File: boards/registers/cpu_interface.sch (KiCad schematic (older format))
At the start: 9 parts, among them J3 IO, U30 74AC20, U31 28C256, U32 62256-TSOP, U33 74ACT02

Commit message: PCB attempt
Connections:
- net a0: now also J3.4 (Pin_4), U32.15 (A2); no longer J3.3 (Pin_3), U32.17 (A0)
- net a1: now also J3.3 (Pin_3); no longer J3.4 (Pin_4)
- net a11: now also U32.5 (A13); no longer U32.2 (A11)
- net a12: now also U32.4 (A8); no longer U32.9 (A12)
- net a13: now also U32.3 (A9); no longer U32.5 (A13)
- net a14: now also U32.2 (A11); no longer U32.8 (A14)
- net a2: now also J3.6 (Pin_6), U32.17 (A0); no longer J3.5 (Pin_5), U32.15 (A2)
- net a3: now also J3.5 (Pin_5); no longer J3.6 (Pin_6)
- net a4: now also J3.8 (Pin_8); no longer J3.7 (Pin_7)
- net a5: now also J3.7 (Pin_7); no longer J3.8 (Pin_8)
- net a6: now also J3.10 (Pin_10); no longer J3.9 (Pin_9)
- net a7: now also J3.9 (Pin_9); no longer J3.10 (Pin_10)
- net a8: now also U32.9 (A12); no longer U32.4 (A8)
- net a9: now also U32.8 (A14); no longer U32.3 (A9)
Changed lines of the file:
@@
 	6000 3200 5550 3200
 Text Label 5650 1800 2    50   ~ 0
-a0
+a2
 Text Label 5550 1900 0    50   ~ 0
 a1
 Text Label 5550 2000 0    50   ~ 0
-a2
+a0
 Text Label 5550 2100 0    50   ~ 0
 a3
@@
 a6
 Text Label 5550 2600 0    50   ~ 0
-a8
+a12
 Text Label 5550 2500 0    50   ~ 0
 a7
 Text Label 5550 2700 0    50   ~ 0
-a9
+a13
 Text Label 5550 2800 0    50   ~ 0
 a10
 Text Label 5550 2900 0    50   ~ 0
+a14
+Text Label 5550 3000 0    50   ~ 0
+a8
+Text Label 5550 3100 0    50   ~ 0
 a11
-Text Label 5550 3000 0    50   ~ 0
-a12
-Text Label 5550 3100 0    50   ~ 0
-a13
 Text Label 5550 3200 0    50   ~ 0
-a14
+a9
 Wire Bus Line
 	5450 1200 2800 1200
@@
 	9200 1800 9450 1800
 Text Label 9250 1500 0    50   ~ 0
+a1
+Text Label 9250 1600 0    50   ~ 0
+a3
+Text Label 9250 1700 0    50   ~ 0
+a5
+Text Label 9250 1800 0    50   ~ 0
+a7
+Text Label 10100 1500 0    50   ~ 0
 a0
-Text Label 9250 1600 0    50   ~ 0
+Text Label 10100 1600 0    50   ~ 0
 a2
-Text Label 9250 1700 0    50   ~ 0
+Text Label 10100 1700 0    50   ~ 0
 a4
-Text Label 9250 1800 0    50   ~ 0
+Text Label 10100 1800 0    50   ~ 0
 a6
-Text Label 10100 1500 0    50   ~ 0
-a1
-Text Label 10100 1600 0    50   ~ 0
-a3
-Text Label 10100 1700 0    50   ~ 0
-a5
-Text Label 10100 1800 0    50   ~ 0
-a7
 $Comp
 L Connector_Generic:Conn_02x13_Odd_Even J3

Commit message: CPU registers board
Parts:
- removed C33: 0.1u, Capacitor_SMD:C_0805_2012Metric, symbol Device:C
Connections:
- net a0: now also J3.17 (Pin_17); no longer J3.4 (Pin_4)
- net a1: now also J3.18 (Pin_18); no longer J3.3 (Pin_3)
- net a2: now also J3.19 (Pin_19); no longer J3.6 (Pin_6)
- net a3: now also J3.20 (Pin_20); no longer J3.5 (Pin_5)
- net a4: now also J3.21 (Pin_21); no longer J3.8 (Pin_8)
- net a5: now also J3.22 (Pin_22); no longer J3.7 (Pin_7)
- net a6: now also J3.23 (Pin_23); no longer J3.10 (Pin_10)
- net a7: now also J3.24 (Pin_24); no longer J3.9 (Pin_9)
- net clk: now also J3.7 (Pin_7); no longer J3.19 (Pin_19)
- net d0: now also J3.16 (Pin_16), U32.26 (D7); no longer J3.11 (Pin_11), U32.18 (D0)
- net d1: now also J3.15 (Pin_15), U32.25 (D6); no longer J3.12 (Pin_12), U32.19 (D1)
- net d2: now also J3.14 (Pin_14), U32.24 (D5); no longer J3.13 (Pin_13), U32.20 (D2)
- net d3: now also J3.13 (Pin_13), U32.23 (D4); no longer J3.14 (Pin_14), U32.22 (D3)
- net d4: now also J3.12 (Pin_12), U32.22 (D3); no longer J3.15 (Pin_15), U32.23 (D4)
- net d5: now also J3.11 (Pin_11), U32.20 (D2); no longer J3.16 (Pin_16), U32.24 (D5)
- net d6: now also J3.10 (Pin_10), U32.19 (D1); no longer J3.17 (Pin_17), U32.25 (D6)
- net d7: now also J3.9 (Pin_9), U32.18 (D0); no longer J3.18 (Pin_18), U32.26 (D7)
- net ~io_cs: now also J3.4 (Pin_4); no longer J3.20 (Pin_20)
- net ~io_rdy: now also J3.3 (Pin_3); no longer J3.24 (Pin_24)
- net ~oe: now also J3.5 (Pin_5); no longer J3.21 (Pin_21)
- net ~rst: now also J3.8 (Pin_8); no longer J3.22 (Pin_22)
- net ~we: now also J3.6 (Pin_6); no longer J3.23 (Pin_23)
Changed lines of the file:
@@
 	7000 2500 7250 2500
 Text Label 7100 1800 0    50   ~ 0
+d7
+Text Label 7100 1900 0    50   ~ 0
+d6
+Text Label 7100 2000 0    50   ~ 0
+d5
+Text Label 7100 2100 0    50   ~ 0
+d4
+Text Label 7100 2200 0    50   ~ 0
+d3
+Text Label 7100 2300 0    50   ~ 0
+d2
+Text Label 7100 2400 0    50   ~ 0
+d1
+Text Label 7100 2500 0    50   ~ 0
 d0
-Text Label 7100 1900 0    50   ~ 0
-d1
-Text Label 7100 2000 0    50   ~ 0
-d2
-Text Label 7100 2100 0    50   ~ 0
-d3
-Text Label 7100 2200 0    50   ~ 0
-d4
-Text Label 7100 2300 0    50   ~ 0
-d5
-Text Label 7100 2400 0    50   ~ 0
-d6
-Text Label 7100 2500 0    50   ~ 0
-d7
 Wire Bus Line
 	7350 1300 4500 1300
@@
 	1    0    0    -1
 $EndComp
-$Comp
-L Device:C C33
-U 1 1 5ECF04C3
-P 9800 4800
-F 0 "C33" H 9915 4846 50  0000 L CNN
-F 1 "0.1u" H 9915 4755 50  0000 L CNN
-F 2 "Capacitor_SMD:C_0805_2012Metric" H 9838 4650 50  0001 C CNN
-F 3 "~" H 9800 4800 50  0001 C CNN
-	1    9800 4800
-	1    0    0    -1
-$EndComp
-$Comp
-L power:VCC #PWR0211
-U 1 1 5ECF04C9
-P 9800 4650
-F 0 "#PWR0211" H 9800 4500 50  0001 C CNN
-F 1 "VCC" H 9817 4823 50  0000 C CNN
-F 2 "" H 9800 4650 50  0001 C CNN
-F 3 "" H 9800 4650 50  0001 C CNN
-	1    9800 4650
-	1    0    0    -1
-$EndComp
-$Comp
-L power:GND #PWR0212
-U 1 1 5ECF04CF
-P 9800 4950
-F 0 "#PWR0212" H 9800 4700 50  0001 C CNN
-F 1 "GND" H 9805 4777 50  0000 C CNN
-F 2 "" H 9800 4950 50  0001 C CNN
-F 3 "" H 9800 4950 50  0001 C CNN
-	1    9800 4950
-	1    0    0    -1
-$EndComp
 Wire Wire Line
 	6450 4900 6450 4800
@@
 	0    1    1    0
 $EndComp
-Text Label 9950 2500 0    50   ~ 0
+Text Label 9450 1500 2    50   ~ 0
 ~io_rdy
-Text Label 9950 2300 0    50   ~ 0
+Text Label 9950 1500 0    50   ~ 0
 ~io_cs
 Text Label 1750 1800 0    50   ~ 0
@@
 Text Label 1500 2100 0    50   ~ 0
 ~rst
-Text Label 9450 2400 2    50   ~ 0
+Text Label 9450 1600 2    50   ~ 0
 ~oe
-Text Label 9450 2500 2    50   ~ 0
+Text Label 9950 1600 0    50   ~ 0
 ~we
-Text Label 9950 2400 0    50   ~ 0
+Text Label 9950 1700 0    50   ~ 0
 ~rst
-Text Label 9450 2300 2    50   ~ 0
+Text Label 9450 1700 2    50   ~ 0
 clk
 Entry Wire Line
-	10300 1600 10400 1500
-Entry Wire Line
-	10300 1500 10400 1400
-Wire Wire Line
-	9950 1500 10300 1500
-Wire Wire Line
-	10300 1600 9950 1600
-Entry Wire Line
-	10300 1800 10400 1700
-Entry Wire Line
-	10300 1700 10400 1600
-Wire Wire Line
-	9950 1700 10300 1700
-Wire Wire Line
-	10300 1800 9950 1800
-Entry Wire Line
-	9100 1600 9200 1500
-Entry Wire Line
-	9100 1700 9200 1600
-Wire Wire Line
-	9450 1500 9200 1500
-Wire Wire Line
-	9200 1600 9450 1600
-Entry Wire Line
-	9100 1800 9200 1700
-Entry Wire Line
-	9100 1900 9200 1800
-Wire Wire Line
-	9450 1700 9200 1700
-Wire Wire Line
-	9200 1800 9450 1800
-Text Label 9250 1500 0    50   ~ 0
+	10300 2300 10400 2200
+Entry Wire Line
+	10300 2200 10400 2100
+Wire Wire Line
+	9950 2200 10300 2200
+Wire Wire Line
+	10300 2300 9950 2300
+Entry Wire Line
+	10300 2500 10400 2400
+Entry Wire Line
+	10300 2400 10400 2300
+Wire Wire Line
+	9950 2400 10300 2400
+Entry Wire Line
+	9100 2300 9200 2200
+Entry Wire Line
+	9100 2400 9200 2300
+Wire Wire Line
+	9450 2200 9200 2200
+Wire Wire Line
+	9200 2300 9450 2300
+Entry Wire Line
+	9100 2500 9200 2400
+Entry Wire Line
+	9100 2600 9200 2500
+Wire Wire Line
+	9450 2400 9200 2400
+Wire Wire Line
+	9200 2500 9450 2500
+Text Label 9250 2200 0    50   ~ 0
+a0
+Text Label 9250 2300 0    50   ~ 0
+a2
+Text Label 9250 2400 0    50   ~ 0
+a4
+Text Label 9250 2500 0    50   ~ 0
+a6
+Text Label 10100 2200 0    50   ~ 0
 a1
-Text Label 9250 1600 0    50   ~ 0
+Text Label 10100 2300 0    50   ~ 0
 a3
-Text Label 9250 1700 0    50   ~ 0
+Text Label 10100 2400 0    50   ~ 0
 a5
-Text Label 9250 1800 0    50   ~ 0
+Text Label 10100 2500 0    50   ~ 0
 a7
-Text Label 10100 1500 0    50   ~ 0
-a0
-Text Label 10100 1600 0    50   ~ 0
-a2
-Text Label 10100 1700 0    50   ~ 0
-a4
-Text Label 10100 1800 0    50   ~ 0
-a6
 $Comp
 L Connector_Generic:Conn_02x13_Odd_Even J3
@@
 	1    0    0    -1
 $EndComp
-Text Label 10100 2200 0    50   ~ 0
+Text Label 10100 2100 0    50   ~ 0
+d0
+Text Label 10100 2000 0    50   ~ 0
+d2
+Text Label 10100 1900 0    50   ~ 0
+d4
+Text Label 10100 1800 0    50   ~ 0
+d6
+Wire Wire Line
+	9950 1800 10300 1800
+Wire Wire Line
+	10300 1900 9950 1900
+Wire Wire Line
+	9950 2000 10300 2000
+Wire Wire Line
+	10300 2100 9950 2100
+Entry Wire Line
+	10300 2100 10400 2000
+Entry Wire Line
+	10300 2000 10400 1900
+Entry Wire Line
+	10300 1900 10400 1800
+Entry Wire Line
+	10300 1800 10400 1700
+Text Label 9250 2100 0    50   ~ 0
+d1
+Text Label 9250 2000 0    50   ~ 0
+d3
+Text Label 9250 1900 0    50   ~ 0
+d5
+Text Label 9250 1800 0    50   ~ 0
 d7
-Text Label 10100 2100 0    50   ~ 0
-d5
-Text Label 10100 2000 0    50   ~ 0
-d3
-Text Label 10100 1900 0    50   ~ 0
-d1
-Wire Wire Line
-	9950 1900 10300 1900
-Wire Wire Line
-	10300 2000 9950 2000
-Wire Wire Line
-	9950 2100 10300 2100
-Wire Wire Line
-	10300 2200 9950 2200
-Entry Wire Line
-	10300 2200 10400 2100
-Entry Wire Line
-	10300 2100 10400 2000
-Entry Wire Line
-	10300 2000 10400 1900
-Entry Wire Line
-	10300 1900 10400 1800
-Text Label 9250 2200 0    50   ~ 0
-d6
-Text Label 9250 2100 0    50   ~ 0
-d4
-Text Label 9250 2000 0    50   ~ 0
-d2
-Text Label 9250 1900 0    50   ~ 0
-d0
-Wire Wire Line
-	9200 2200 9450 2200
-Wire Wire Line
-	9450 2100 9200 2100
-Wire Wire Line
-	9200 2000 9450 2000
-Wire Wire Line
-	9450 1900 9200 1900
+Wire Wire Line
+	9200 2100 9450 2100
+Wire Wire Line
+	9450 2000 9200 2000
+Wire Wire Line
+	9200 1900 9450 1900
+Wire Wire Line
+	9450 1800 9200 1800
+Entry Wire Line
+	9100 1900 9200 1800
 Entry Wire Line
 	9100 2000 9200 1900
@@
 Entry Wire Line
 	9100 2200 9200 2100
-Entry Wire Line
-	9100 2300 9200 2200
 Wire Bus Line
 	10400 1100 9100 1100
@@
 	9100 1100 9100 1200
 Connection ~ 5450 1200
-Connection ~ 9100 1200
-Wire Bus Line
-	10400 2750 9100 2750
-Wire Bus Line
-	9100 2000 7350 2000
-Connection ~ 7350 2000
-Wire Bus Line
-	10400 1100 10400 1700
-Wire Bus Line
-	7350 1300 7350 2000
-Wire Bus Line
-	9100 1200 9100 1900
-Wire Bus Line
-	10400 1800 10400 2750
-Wire Bus Line
-	9100 2000 9100 2750
-Wire Bus Line
-	7350 2000 7350 2400
+Wire Wire Line
+	9950 2500 10300 2500
 Wire Bus Line
 	4500 1300 4500 2350
 Wire Bus Line
+	7350 1300 7350 2400
+Wire Bus Line
 	5450 1200 5450 3300

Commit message: PLCC-32 socket footprint
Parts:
- removed U31: 28C256, Package_LCC:PLCC-28_SMD-Socket, symbol Memory_EEPROM:28C256
- added U31: AT28C256-PLCC32, missing:PLCC-32_SMD_Socket, symbol missing:AT28C256-PLCC32
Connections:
- net GND: now also U31.16 (GND)
- net VCC: now also U31.31 (~WE), U31.32 (VCC)
- net a0: now also U31.11 (A0)
- net a1: now also U31.10 (A1)
- net a10: now also U31.24 (A10)
- net a11: now also U31.27 (A11)
- net a12: now also U31.3 (A12)
- net a13: now also U31.30 (A13)
- net a14: now also U31.2 (A14)
- net a15: now also U31.23 (~CE)
- net a2: now also U31.9 (A2)
- net a3: now also U31.8 (A3)
- net a4: now also U31.7 (A4)
- net a5: now also U31.6 (A5)
- net a6: now also U31.5 (A6)
- net a7: now also U31.4 (A7)
- net a8: now also U31.29 (A8)
- net a9: now also U31.28 (A9)
- net d0: now also U31.13 (IO0)
- net d1: now also U31.14 (IO1)
- net d2: now also U31.15 (IO2)
- net d3: now also U31.18 (IO3)
- net d4: now also U31.19 (IO4)
- net d5: now also U31.20 (IO5)
- net d6: now also U31.21 (IO6)
- net d7: now also U31.22 (IO7)
- net ~oe: now also U31.25 (~OE)
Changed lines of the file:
@@
 0000-7FFF - ROM\n8000-EFFF - RAM\nF000-FFFF - IO
-$Comp
-L Memory_EEPROM:28C256 U31
-U 1 1 5EC757DC
-P 3750 2650
-F 0 "U31" H 4150 1700 50  0000 C CNN
-F 1 "28C256" H 4100 1600 50  0000 C CNN
-F 2 "Package_LCC:PLCC-28_SMD-Socket" H 3750 2650 50  0001 C CNN
-F 3 "http://ww1.microchip.com/downloads/en/DeviceDoc/doc0006.pdf" H 3750 2650 50  0001 C CNN
-	1    3750 2650
-	1    0    0    -1
-$EndComp
 $Comp
 L power:GND #PWR0198
@@
 	2900 3550 3350 3550
 Wire Wire Line
-	2500 3450 2500 1700
-Wire Wire Line
 	2500 1700 1500 1700
-Wire Wire Line
-	2500 3450 3350 3450
 Text Label 3000 1750 2    50   ~ 0
 a0
@@
 	2800 1200 1500 1200
 Wire Wire Line
-	2500 3450 2500 4000
-Wire Wire Line
 	2500 4000 5450 4000
 Wire Wire Line
@@
 Wire Wire Line
 	5450 3500 6000 3500
-Connection ~ 2500 3450
 Wire Wire Line
 	1500 1800 2400 1800
@@
 L power:VCC #PWR0194
 U 1 1 5ED0A785
-P 3350 3350
-F 0 "#PWR0194" H 3350 3200 50  0001 C CNN
-F 1 "VCC" V 3368 3477 50  0000 L CNN
-F 2 "" H 3350 3350 50  0001 C CNN
-F 3 "" H 3350 3350 50  0001 C CNN
-	1    3350 3350
+P 3350 3450
+F 0 "#PWR0194" H 3350 3300 50  0001 C CNN
+F 1 "VCC" V 3368 3577 50  0000 L CNN
+F 2 "" H 3350 3450 50  0001 C CNN
+F 3 "" H 3350 3450 50  0001 C CNN
+	1    3350 3450
 	0    -1   -1   0
 $EndComp
@@
 Wire Wire Line
 	9950 2500 10300 2500
+$Comp
+L missing:AT28C256-PLCC32 U31
+U 1 1 6014E21E
+P 3750 2650
+F 0 "U31" H 4150 1650 50  0000 C CNN
+F 1 "AT28C256-PLCC32" H 4350 1550 50  0000 C CNN
+F 2 "missing:PLCC-32_SMD_Socket" H 4000 3000 50  0001 C CNN
+F 3 "http://ww1.microchip.com/downloads/en/DeviceDoc/doc0006.pdf" H 4000 3000 50  0001 C CNN
+	1    3750 2650
+	1    0    0    -1
+$EndComp
+Wire Wire Line
+	2500 1700 2500 3350
+Wire Wire Line
+	3350 3350 2500 3350
 Wire Bus Line
 	4500 1300 4500 2350
@@
 Wire Bus Line
 	2800 1200 2800 5600
+Connection ~ 2500 3350
+Wire Wire Line
+	2500 3350 2500 4000
 $EndSCHEMATC

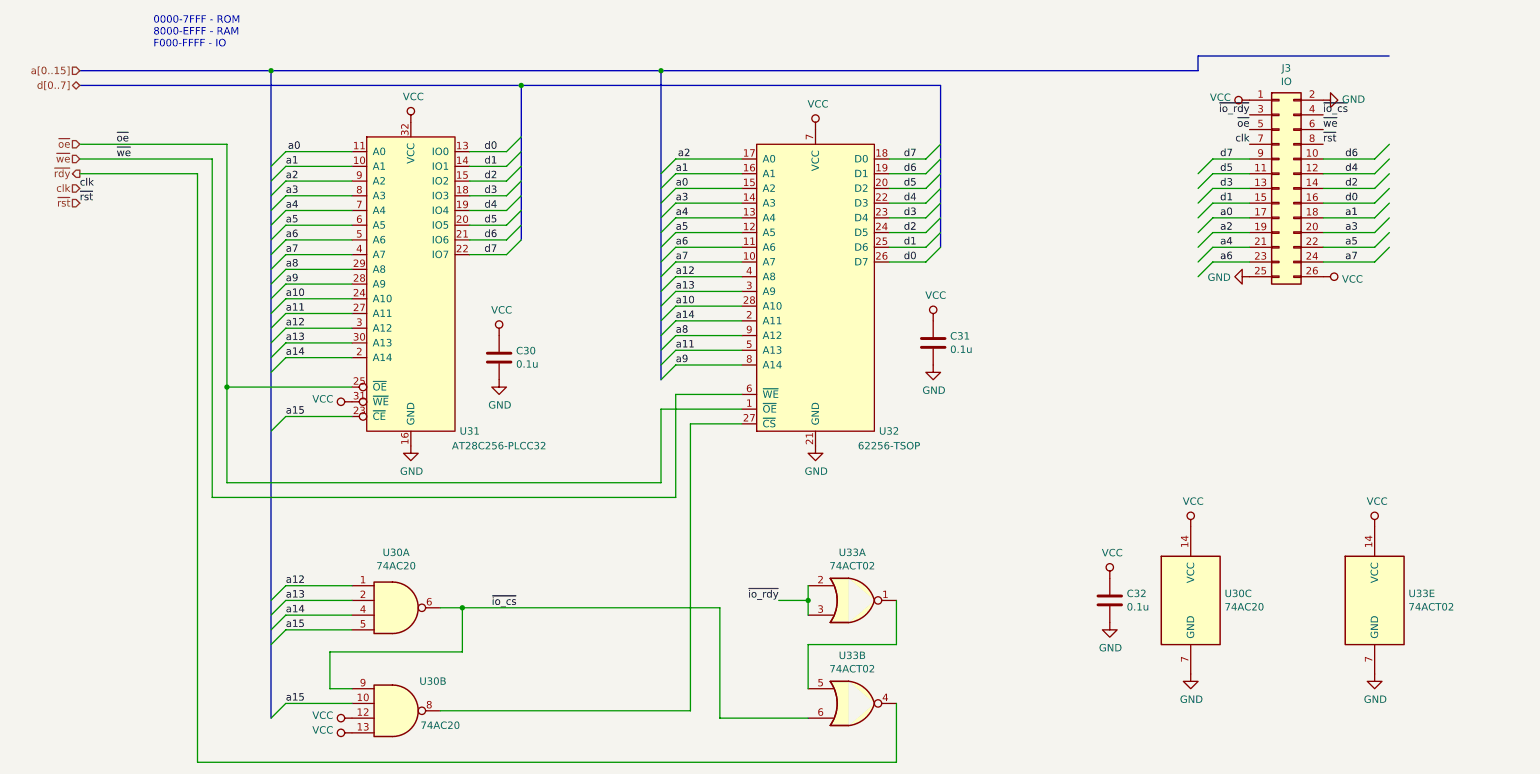
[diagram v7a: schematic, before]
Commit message: Remove RAM and ROM from the registers board, board rework in progress
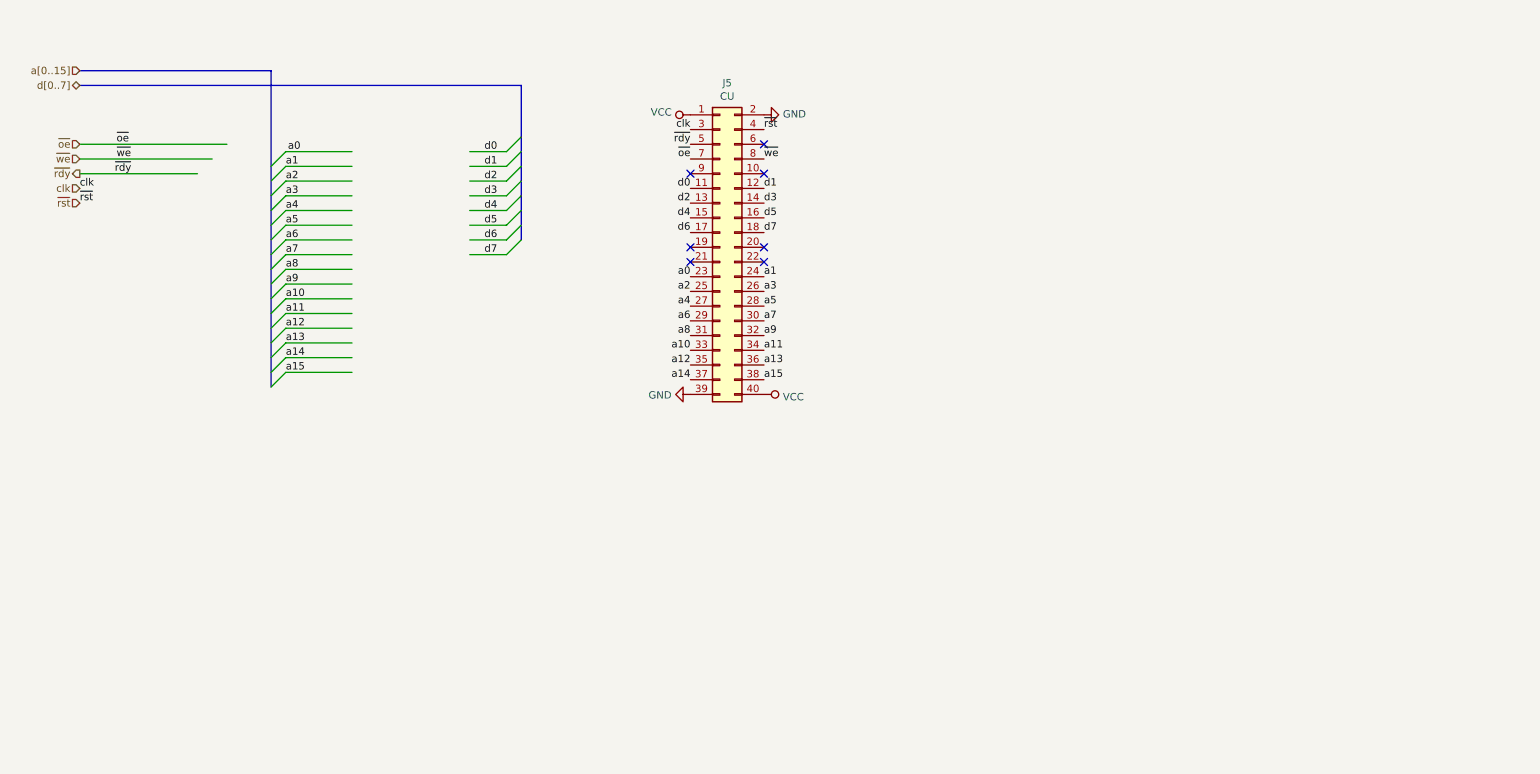
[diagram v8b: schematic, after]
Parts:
- removed C30, C31, C32: 0.1u, Capacitor_SMD:C_0805_2012Metric, symbol Device:C
- removed J3: IO, Connector_PinSocket_2.54mm:PinSocket_2x13_P2.54mm_Horizontal, symbol Connector_Generic:Conn_02x13_Odd_Even
- removed U30: 74AC20, Package_SO:SOIC-14_3.9x8.7mm_P1.27mm, symbol 74xx:74LS20
- removed U31: AT28C256-PLCC32, missing:PLCC-32_SMD_Socket, symbol missing:AT28C256-PLCC32
- removed U32: 62256-TSOP, Package_SO:TSOP-I-28_11.8x8mm_P0.55mm, symbol missing:62256-TSOP
- removed U33: 74ACT02, Package_SO:TSSOP-14_4.4x5mm_P0.65mm, symbol 74xx:74LS02
- added J5: CU, Connector_PinSocket_2.54mm:PinSocket_2x20_P2.54mm_Horizontal, symbol Connector_Generic:Conn_02x20_Odd_Even
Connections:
- net labels removed: ~io_cs, ~io_rdy
- wire segments 101 -> 27
- no-connect marks 0 -> 7
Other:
- note removed: "0000-7FFF - ROM\n8000-EFFF - RAM\nF000-FFFF - IO"
